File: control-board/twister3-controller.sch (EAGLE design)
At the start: 54 parts, among them J2 OSTVN04A150, J7 BARREL-JACK_PJ-063BH, U1 MAX6816, U10 Teensy 3.2, U11 TMC2130-LA, U2 GDM1602K, U3 IS31FL3193, U4 MIC4680-5.0YM-TR

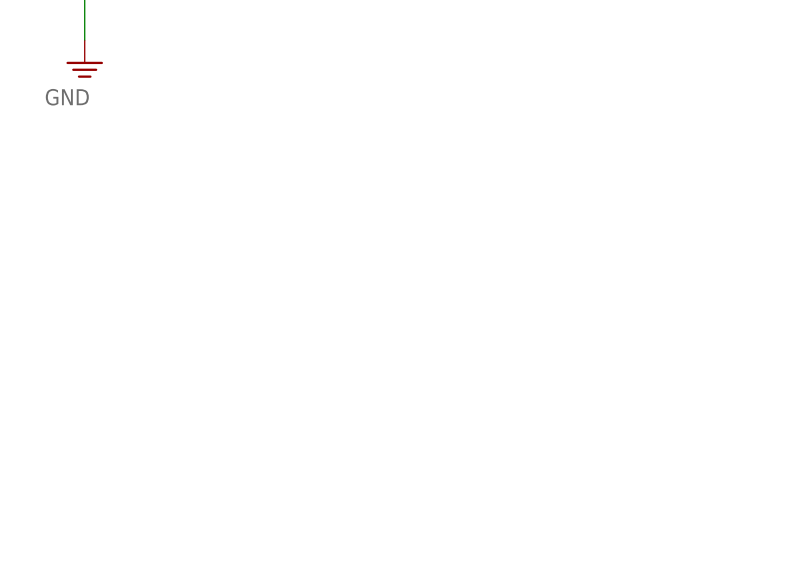
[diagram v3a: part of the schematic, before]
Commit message: Small updates to control board
- Tighter tolerance on LCD cutout
- Added test points
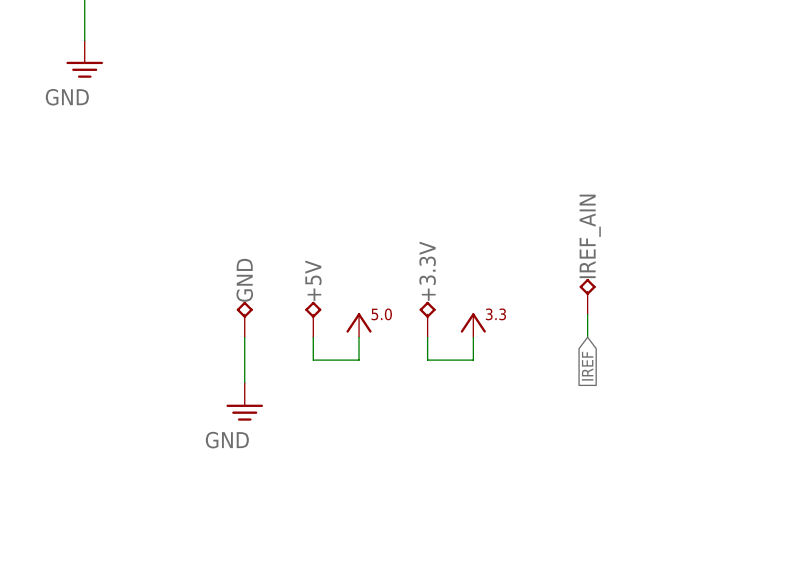
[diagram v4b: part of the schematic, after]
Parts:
- added +3.3V, +5V, GND, IREF_AIN: (no value), jonnew:TP_2MM
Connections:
- net +3V3: now also +3.3V.TP
- net +5V0: now also +5V.TP
- net GND: now also GND.TP
- net IREF: now also IREF_AIN.TP
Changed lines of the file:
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@@
 <part name="SUPPLY17" library="jonnew" deviceset="GND" device=""/>
 <part name="SUPPLY22" library="jonnew" deviceset="GND" device=""/>
+<part name="GND" library="jonnew" deviceset="TP" device="_2MM"/>
+<part name="+5V" library="jonnew" deviceset="TP" device="_2MM"/>
+<part name="+3.3V" library="jonnew" deviceset="TP" device="_2MM"/>
+<part name="IREF_AIN" library="jonnew" deviceset="TP" device="_2MM"/>
+<part name="SUPPLY24" library="jonnew" deviceset="GND" device=""/>
+<part name="P+3" library="jonnew" deviceset="+5V" device=""/>
+<part name="SUPPLY27" library="jonnew" deviceset="+3V3" device=""/>
 </parts>
 <sheets>
@@
 <instance part="SUPPLY17" gate="PE" x="431.8" y="66.04"/>
 <instance part="SUPPLY22" gate="PE" x="439.42" y="66.04"/>
+<instance part="GND" gate="G$1" x="251.46" y="33.02"/>
+<instance part="+5V" gate="G$1" x="259.08" y="33.02"/>
+<instance part="+3.3V" gate="G$1" x="271.78" y="33.02"/>
+<instance part="IREF_AIN" gate="G$1" x="289.56" y="35.56"/>
+<instance part="SUPPLY24" gate="PE" x="251.46" y="22.86"/>
+<instance part="P+3" gate="1" x="264.16" y="33.02"/>
+<instance part="SUPPLY27" gate="PWR1" x="276.86" y="30.48"/>
 </instances>
 <busses>
@@
 <pinref part="C13" gate="C" pin="2"/>
 <pinref part="U11" gate="IC" pin="VCC_IO"/>
+</segment>
+<segment>
+<pinref part="+3.3V" gate="G$1" pin="TP"/>
+<wire x1="271.78" y1="30.48" x2="271.78" y2="27.94" width="0.1524" layer="91"/>
+<wire x1="271.78" y1="27.94" x2="276.86" y2="27.94" width="0.1524" layer="91"/>
+<pinref part="SUPPLY27" gate="PWR1" pin="+3V3"/>
+<wire x1="276.86" y1="27.94" x2="276.86" y2="30.48" width="0.1524" layer="91"/>
 </segment>
 </net>
@@
 <wire x1="439.42" y1="86.36" x2="439.42" y2="68.58" width="0.1524" layer="91"/>
 </segment>
+<segment>
+<pinref part="GND" gate="G$1" pin="TP"/>
+<pinref part="SUPPLY24" gate="PE" pin="GND"/>
+<wire x1="251.46" y1="30.48" x2="251.46" y2="25.4" width="0.1524" layer="91"/>
+</segment>
 </net>
 <net name="ENC_A" class="0">
@@
 <pinref part="U11" gate="IC" pin="AIN_IREF"/>
 <pinref part="R10" gate="1" pin="W"/>
+</segment>
+<segment>
+<pinref part="IREF_AIN" gate="G$1" pin="TP"/>
+<wire x1="289.56" y1="33.02" x2="289.56" y2="30.48" width="0.1524" layer="91"/>
+<label x="289.56" y="30.48" size="1.27" layer="95" rot="R270" xref="yes"/>
 </segment>
 </net>
@@
 <pinref part="P+17" gate="1" pin="+5V0"/>
 </segment>
-</net>
+<segment>
+<pinref part="+5V" gate="G$1" pin="TP"/>
+<wire x1="259.08" y1="30.48" x2="259.08" y2="27.94" width="0.1524" layer="91"/>
+<wire x1="259.08" y1="27.94" x2="264.16" y2="27.94" width="0.1524" layer="91"/>
+<wire x1="264.16" y1="27.94" x2="264.16" y2="30.48" width="0.1524" layer="91"/>
+<pinref part="P+3" gate="1" pin="+5V0"/>
+</segment>
+</net>

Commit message: Updates to control board after assembly of rev 1.1
- Better retaining mechanism for top panel
- Simplified and updated BOM on the google doc to match this version
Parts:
- removed C17: 100n/50V, jonnew:C_0402
- removed C18: 100nF/50V, jonnew:C_0402
- removed C19: 22nF/50V, jonnew:C_0402
- removed R18, R19: 0.11, jonnew:R_0805
- removed R22: 20k, jonnew:R_0603
- removed R23: 2.2, jonnew:R_0402
- removed U11: TMC2130-LA, we-chip:TMC21X0-LA
- added C10, C9: 100nF/50V, jonnew:C_0603
- added C11: 1uF/50V, jonnew:C_0603
- added R11: 4.7k, cyclops:R_0603
- added R17: 10k, jonnew:R_0603
- added R8: 20k, jonnew:TRIM_US-SM-42/43X
- added R9: 4.7k, jonnew:R_0603
- added U6: GDM1602K, jonnew:LCD-16X2SILK
- C12: value 1u/50V -> 100nF/50V
- C13: value 100n/50V -> 22nF/50V
- C14: value 470nF/10V -> 1uF/50V; device jonnew:C_0402 -> jonnew:C_0603
- C15: value 47uF/10V -> 100nF/50V; device jonnew:C_0402 -> jonnew:C_0603
- C16: value 100n/50V -> 470nF/10V
- C3: value 10nF -> 1uF/50V
- C4: value 10nF -> T491D156K035AT; device jonnew:C_0603 -> jonnew:C-POL_7343M
- C5: value 10nF -> T491D227M010AT; device jonnew:C_0603 -> jonnew:C-POL_7343M
- C6: value 1uF -> 10nF
- C7: value T491D227M010AT -> 10nF; device jonnew:C-POL_7343M -> jonnew:C_0603
- C8: value T491D156K035AT -> 10nF; device jonnew:C-POL_7343M -> jonnew:C_0603
- J1: value (none) -> BARREL-JACK_PJ-063BH; device jonnew:PINHD-1X4 -> jonnew:BARREL-JACK_PJ-063BH
- J2: value OSTVN04A150 -> (none)
- J5: value (none) -> OSTVN04A150; device jonnew:PINHD-1X4_SMD-0.1" -> jonnew:PINHD-1X4
- J7: value BARREL-JACK_PJ-063BH -> (none); device jonnew:BARREL-JACK_PJ-063BH -> jonnew:PINHD-1X4
- J8: device jonnew:PINHD-1X4 -> jonnew:PINHD-1X4_SMD-0.1"
- R1: value 10k -> 4.7k
- R10: value 20k -> 4.7k; device jonnew:TRIM_US-SM-42/43X -> jonnew:R_0603
- R12: device jonnew:R_0603 -> cyclops:R_0603
- R13: value 470 -> 20k; device cyclops:R_0603 -> jonnew:R_0603
- R14, R15: value 4.7k -> 0.11; device cyclops:R_0603 -> jonnew:R_0805
- R16: value 100k -> 20k; device jonnew:R_0603 -> jonnew:TRIM_US-SM-42/43X
- R2: value 20k -> 10k; device jonnew:TRIM_US-SM-42/43X -> jonnew:R_0603
- R3: value 4.7k -> 10k
- R6: value 10k -> 470; device jonnew:R_0603 -> cyclops:R_0603
- R7: value 4.7k -> 2.2; device jonnew:R_0603 -> jonnew:R_0402
- U1: value MAX6816 -> IS31FL3193; device jonnew:MAX6816 -> jonnew:IS31FL3193
- U2: value GDM1602K -> MIC4680-5.0YM-TR; device jonnew:LCD-16X2SILK -> jonnew:MIC4680_SOIC
- U3: value IS31FL3193 -> MAX6816; device jonnew:IS31FL3193 -> jonnew:MAX6816
- U4: value MIC4680-5.0YM-TR -> TMC2130-LA; device jonnew:MIC4680_SOIC -> we-chip:TMC21X0-LA
- renumbered J9 to J6, JP6 to J10, JP7 to J11, U10 to U5
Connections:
- net !IS31_SHDN: now also R17.1, U1.!SHDN; no longer R16.1, U3.!SHDN
- net +24V0: now also C10.1, C11.1, C4.+, C9.1, J1.IN, U2.VIN, U4.VS, U4.VSA; no longer C16.1, C17.1, C18.1, C8.+, J7.IN, U11.VS, U11.VSA, U4.VIN
- net +3V3: now also C15.2, U4.VCC_IO; no longer C13.2, U11.VCC_IO
- net +5V0: now also C2.1, C3.1, C5.+, C8.1, R10.1, R11.2, R2.2, R3.2, R8.A, R9.1, U2.FB, U6.A, U6.VDD; no longer C4.1, C5.1, C6.1, C7.+, R14.2, R15.2, R2.A, R3.1, R6.2, R7.1, U2.A, U2.VDD, U4.FB
- net +5VOUT: now also C14.2, R13.2, R7.2, U4.5VOUT; no longer C15.2, R22.2, R23.2, U11.5VOUT
- net BRA1: now also R15.2, U4.BRA; no longer R19.2, U11.BRA
- net BRB1: now also R14.2, U4.BRB; no longer R18.2, U11.BRB
- net BUTT: now also U3.OUT; no longer U1.OUT
- net CFG-0/MISO: now also U4.SDO_NAO_CFG0; no longer U11.SDO_NAO_CFG0
- net CFG-1/MOSI: now also U4.SDI_NAI_CFG1; no longer U11.SDI_NAI_CFG1
- net CFG-2/SCLK: now also U4.SCK_CFG2; no longer U11.SCK_CFG2
- net CFG-3/!TMC_CS: now also U4.CSN_CFG3; no longer U11.CSN_CFG3
- net CFG-6: now also U4.DRV_ENN_CFG6; no longer U11.DRV_ENN_CFG6
- net CFG4: now also U4.ENCB_DCEN_CFG4; no longer U11.ENCB_DCEN_CFG4
- net CFG5: now also U4.ENCA_DCIN_CFG5; no longer U11.ENCA_DCIN_CFG5
- net CPI1: now also C13.2, U4.CPI; no longer C19.2, U11.CPI
- net CPO1: now also C13.1, U4.CPO; no longer C19.1, U11.CPO
- net DB0: now also U6.DB0; no longer U2.DB0
- net DB1: now also U6.DB1; no longer U2.DB1
- net DB2: now also U6.DB2; no longer U2.DB2
- net DB3: now also U6.DB3; no longer U2.DB3
- net DB4: now also U6.DB4; no longer U2.DB4
- net DB5: now also U6.DB5; no longer U2.DB5
- net DB6: now also U6.DB6; no longer U2.DB6
- net DB7: now also U6.DB7; no longer U2.DB7
- net DIAG0: now also R11.1, U4.SWN_DIAG0; no longer R15.1, U11.SWN_DIAG0
- net DIAG1: now also R12.1, U4.SWP_DIAG1; no longer R14.1, U11.SWP_DIAG1
- net DIR: now also U4.REFR_DIR; no longer U11.REFR_DIR
- net E: now also U6.E; no longer U2.E
- net ENC_A: now also C6.1, R4.2; no longer C3.1, R5.2
- net ENC_B: now also C7.1, R5.2; no longer C2.1, R4.2
- net GND: now also C10.2, C11.2, C16.1, C4.-, C5.-, C7.2, C8.2, C9.2, J1.OUT, R14.1, R15.1, R16.E, R17.2, R6.1, R8.E, U1.AD, U2.GND, U2.SHDN, U4.CLK, U4.GNDA, U4.TST_MODE, U6.K, U6.VSS; no longer C12.2, C13.1, C16.2, C17.2, C4.2, C5.2, C7.-, C8.-, J7.OUT, R10.E, R13.1, R16.2, R18.1, R19.1, R2.E, U11.CLK, U11.GND, U11.GNDA, U11.TST_MODE, U2.K, U2.VSS, U3.AD, U4.SHDN
- net IREF: now also R16.W, U4.AIN_IREF; no longer R10.W, U11.AIN_IREF
- net MECH: now also J3.1, J3.2, J3.3, J3.4; no longer J5.1, J5.2, J5.3, J5.4
- net N$1: now also R2.1, R4.1; no longer R1.1, R5.1
- net N$10: now also U1.OUT2; no longer U3.OUT2
- net N$11: now also R8.W, U6.VO; no longer R2.W, U2.VO
- net N$2: now also R6.2, U3.IN; no longer R13.2, U1.IN
- net N$3: now also U1.OUT1; no longer U3.OUT1
- net N$4: now also R3.1, R5.1; no longer R4.1, R6.1
- net N$6: now also J5.1, J8.4; no longer J2.1, J3.4
- net N$7: now also J5.2, J8.3; no longer J2.2, J3.3
- net N$8: now also J5.3, J8.2; no longer J2.3, J3.2
- net N$9: now also J5.4, J8.1; no longer J2.4, J3.1
- net OA1: now also J2.2, U4.OA1; no longer J1.2, U11.OA1
- net OA2: now also J2.1, U4.OA2; no longer J1.1, U11.OA2
- net OB1: now also J2.3, U4.OB1; no longer J1.3, U11.OB1
- net OB2: now also J2.4, U4.OB2; no longer J1.4, U11.OB2
- net RS: now also U6.RS; no longer U2.RS
- net RW: now also U6.R/W; no longer U2.R/W
- net SCL: now also R10.2, U1.SCL; no longer R7.2, U3.SCL
- net SDA: now also R9.2, U1.SDA; no longer R3.2, U3.SDA
- net SD_MODE: now also U4.SD_MODE; no longer U11.SD_MODE
- net SPI_MODE: now also U4.SPI_MODE; no longer U11.SPI_MODE
- net STEP: now also U4.REFL_STEP; no longer U11.REFL_STEP
- net SUPPY4: now also U1.OUT3; no longer U3.OUT3
- net SW: now also U2.SW; no longer U4.SW
- net VCC1: now also C16.2, R7.1, U4.VCC; no longer C14.2, R23.1, U11.VCC
- net VCP1: now also C12.2, U4.VCP; no longer C18.2, U11.VCP
- net VREF2: now also R13.1, R16.A; no longer R10.A, R22.1
- net V_BM: now also R1.1, U1.V_BM; no longer R12.1, U3.V_BM
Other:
- moved on the sheet: C12, C13, C14, C15, C16, C2, C3, C4, C5, C6, C7, C8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
